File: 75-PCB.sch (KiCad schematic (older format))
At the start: 192 parts

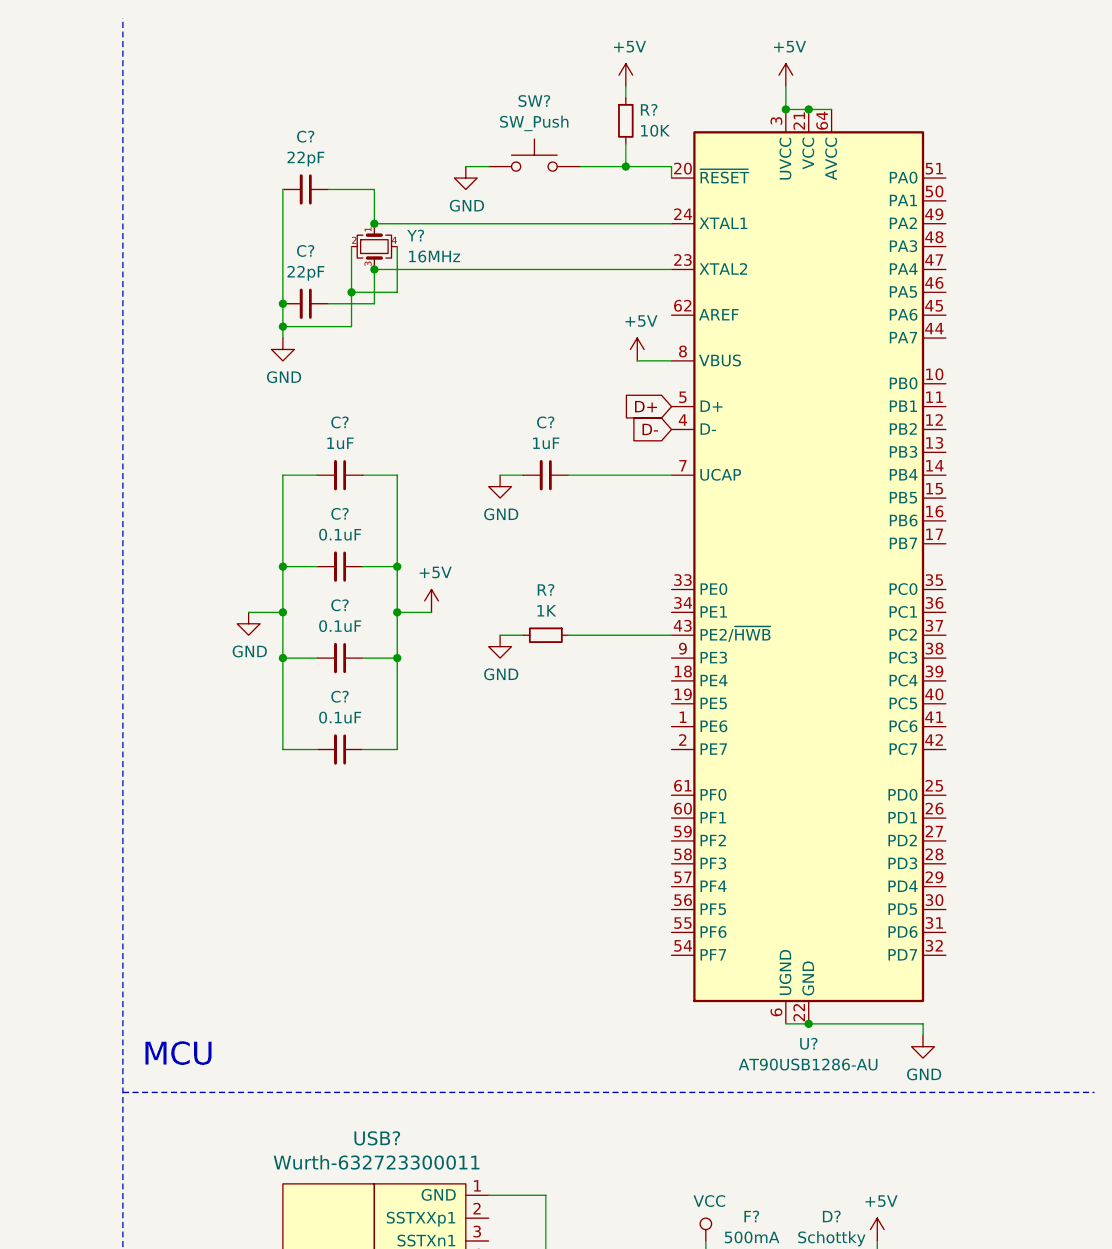
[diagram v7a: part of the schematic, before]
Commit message: Added ISP to schematic
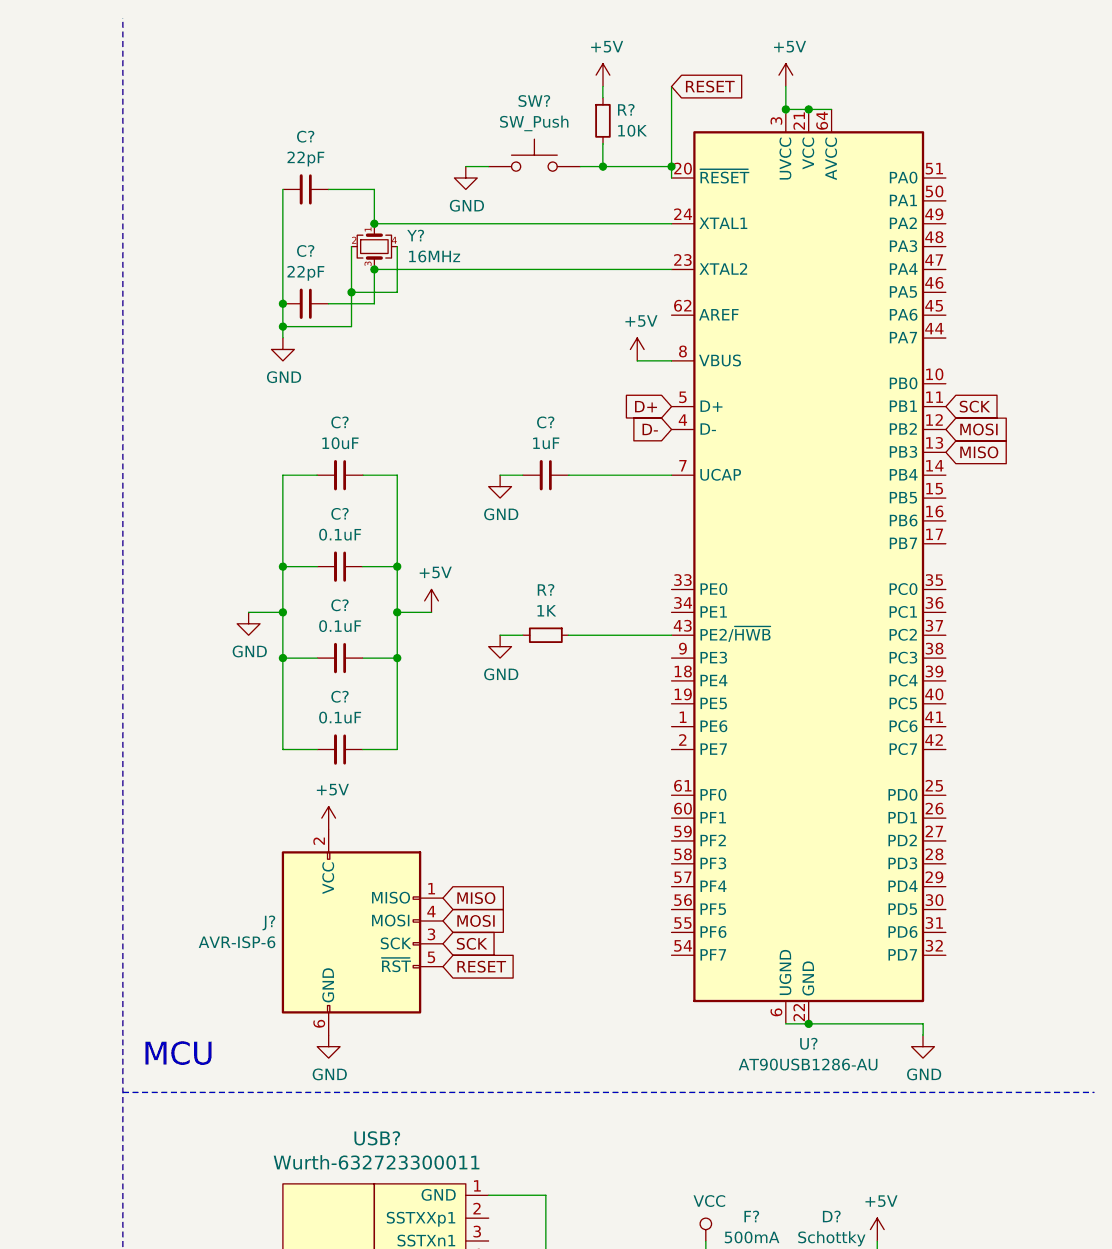
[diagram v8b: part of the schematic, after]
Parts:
- added J?: AVR-ISP-6, symbol Connector:AVR-ISP-6
- C?: value 1uF -> 10uF
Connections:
- net +5V: now also J?.2 (VCC)
- net GND: now also J?.6 (GND)
- net SCK: now reaches U?.11 (PB1)
- net SCK: now also J?.3 (SCK)
- net MOSI: now reaches U?.12 (PB2)
- net MOSI: now also J?.4 (MOSI)
- net MISO: now reaches U?.13 (PB3)
- net MISO: now also J?.1 (MISO)
- net RESET: now reaches R?.2, SW?.2, U?.20 (~RESET)
- net RESET: now also J?.5 (~RST)
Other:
- moved on the sheet: R?
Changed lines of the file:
@@
 P 12750 2500
 F 0 "C?" V 12521 2500 50  0000 C CNN
-F 1 "1uF" V 12612 2500 50  0000 C CNN
+F 1 "10uF" V 12612 2500 50  0000 C CNN
 F 2 "" H 12750 2500 50  0001 C CNN
 F 3 "~" H 12750 2500 50  0001 C CNN
@@
 L Device:R_Small R?
 U 1 1 5EBFBB99
-P 14000 950
-F 0 "R?" H 14059 996 50  0000 L CNN
-F 1 "10K" H 14059 905 50  0000 L CNN
-F 2 "" H 14000 950 50  0001 C CNN
-F 3 "~" H 14000 950 50  0001 C CNN
-	1    14000 950
+P 13900 950
+F 0 "R?" H 13959 996 50  0000 L CNN
+F 1 "10K" H 13959 905 50  0000 L CNN
+F 2 "" H 13900 950 50  0001 C CNN
+F 3 "~" H 13900 950 50  0001 C CNN
+	1    13900 950
 	1    0    0    -1
 $EndComp
@@
 L power:+5V #PWR?
 U 1 1 5EBFBB9F
-P 14000 800
-F 0 "#PWR?" H 14000 650 50  0001 C CNN
-F 1 "+5V" H 14015 973 50  0000 C CNN
-F 2 "" H 14000 800 50  0001 C CNN
-F 3 "" H 14000 800 50  0001 C CNN
-	1    14000 800
+P 13900 800
+F 0 "#PWR?" H 13900 650 50  0001 C CNN
+F 1 "+5V" H 13915 973 50  0000 C CNN
+F 2 "" H 13900 800 50  0001 C CNN
+F 3 "" H 13900 800 50  0001 C CNN
+	1    13900 800
 	1    0    0    -1
 $EndComp
@@
 	13300 1150 13400 1150
 Wire Wire Line
-	14200 1150 14000 1150
+	13900 800  13900 850
 Wire Wire Line
-	14000 800  14000 850
-Wire Wire Line
-	14000 1050 14000 1150
-Connection ~ 14000 1150
-Wire Wire Line
-	14000 1150 13800 1150
+	13900 1050 13900 1150
 Wire Wire Line
 	14200 1200 14200 1150
@@
 Wire Wire Line
 	13550 3200 13450 3200
+$Comp
+L Connector:AVR-ISP-6 J?
+U 1 1 5F5F6B62
+P 12800 4550
+F 0 "J?" H 12471 4646 50  0000 R CNN
+F 1 "AVR-ISP-6" H 12471 4555 50  0000 R CNN
+F 2 "" V 12550 4600 50  0001 C CNN
+F 3 " ~" H 11525 4000 50  0001 C CNN
+	1    12800 4550
+	1    0    0    -1
+$EndComp
+$Comp
+L power:+5V #PWR?
+U 1 1 5F5F99D8
+P 12700 4050
+F 0 "#PWR?" H 12700 3900 50  0001 C CNN
+F 1 "+5V" H 12715 4223 50  0000 C CNN
+F 2 "" H 12700 4050 50  0001 C CNN
+F 3 "" H 12700 4050 50  0001 C CNN
+	1    12700 4050
+	1    0    0    -1
+$EndComp
+$Comp
+L power:GND #PWR?
+U 1 1 5F5FB4A7
+P 12700 4950
+F 0 "#PWR?" H 12700 4700 50  0001 C CNN
+F 1 "GND" H 12705 4777 50  0000 C CNN
+F 2 "" H 12700 4950 50  0001 C CNN
+F 3 "" H 12700 4950 50  0001 C CNN
+	1    12700 4950
+	1    0    0    -1
+$EndComp
+Text GLabel 13200 4350 2    50   Input ~ 0
+MISO
+Text GLabel 13200 4450 2    50   Input ~ 0
+MOSI
+Text GLabel 13200 4550 2    50   Input ~ 0
+SCK
+Text GLabel 13200 4650 2    50   Input ~ 0
+RESET
+Text GLabel 14200 800  2    50   Input ~ 0
+RESET
+Connection ~ 13900 1150
+Wire Wire Line
+	13900 1150 13800 1150
+Wire Wire Line
+	13900 1150 14200 1150
+Wire Wire Line
+	14200 800  14200 1150
+Connection ~ 14200 1150
+Text GLabel 15400 2200 2    50   Input ~ 0
+SCK
+Text GLabel 15400 2300 2    50   Input ~ 0
+MOSI
+Text GLabel 15400 2400 2    50   Input ~ 0
+MISO
 $EndSCHEMATC
